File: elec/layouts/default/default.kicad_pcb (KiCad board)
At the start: 2 copper layers, 46.5 x 25.5 mm, 10 parts

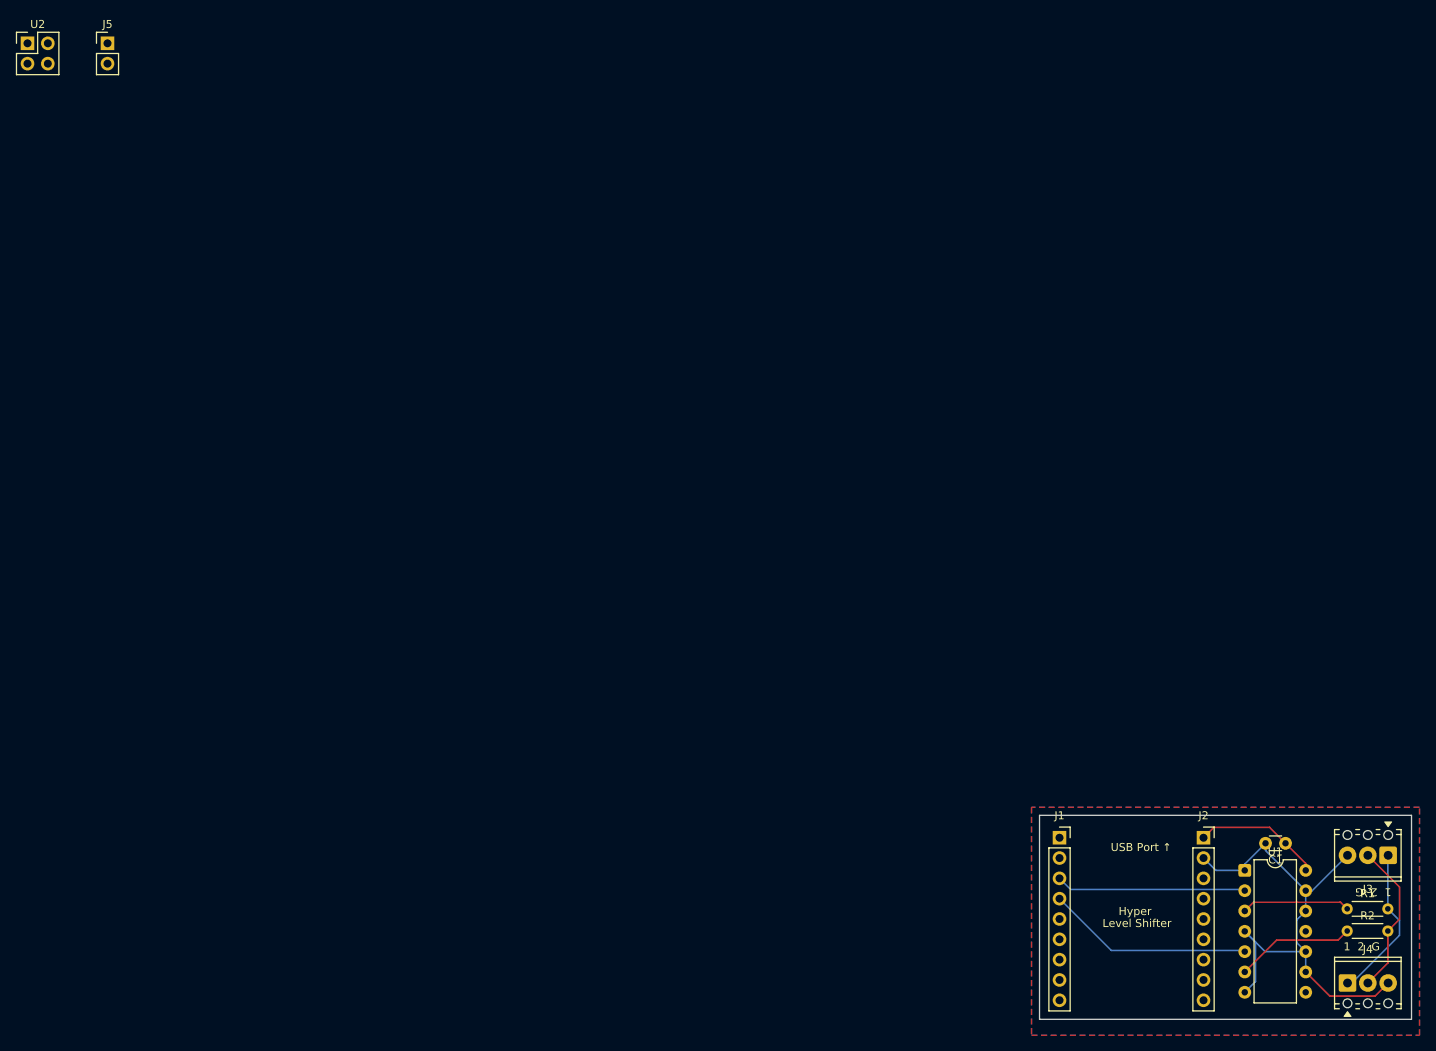
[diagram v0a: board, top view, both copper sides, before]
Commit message: PCB layout fixes, copper fill removal, and back silkscreen artwork
- Fix ESP32 header spacing: J1/J2 corrected to 15.5mm center-to-center
  (was 18mm, which matched castellated pads not through-hole pin rows)
- Shift J1/J2 right by 2.5mm to restore original gap to U1
- Remove GND copper fill (both layers) to fix WiFi antenna detuning
- Move J3/J4 screw terminals 1mm inward to clear silkscreen label overlap
- Update CLAUDE.md with corrected header spacing notes
- Add HyperHDR logo SVG (potrace-traced, evenodd fill) for B.SilkS import
- Back silkscreen text: "Hyper / ESP32 S3 / Level Shifter" between headers

Co-Authored-By: Claude Sonnet 4.6 <noreply@anthropic.com>
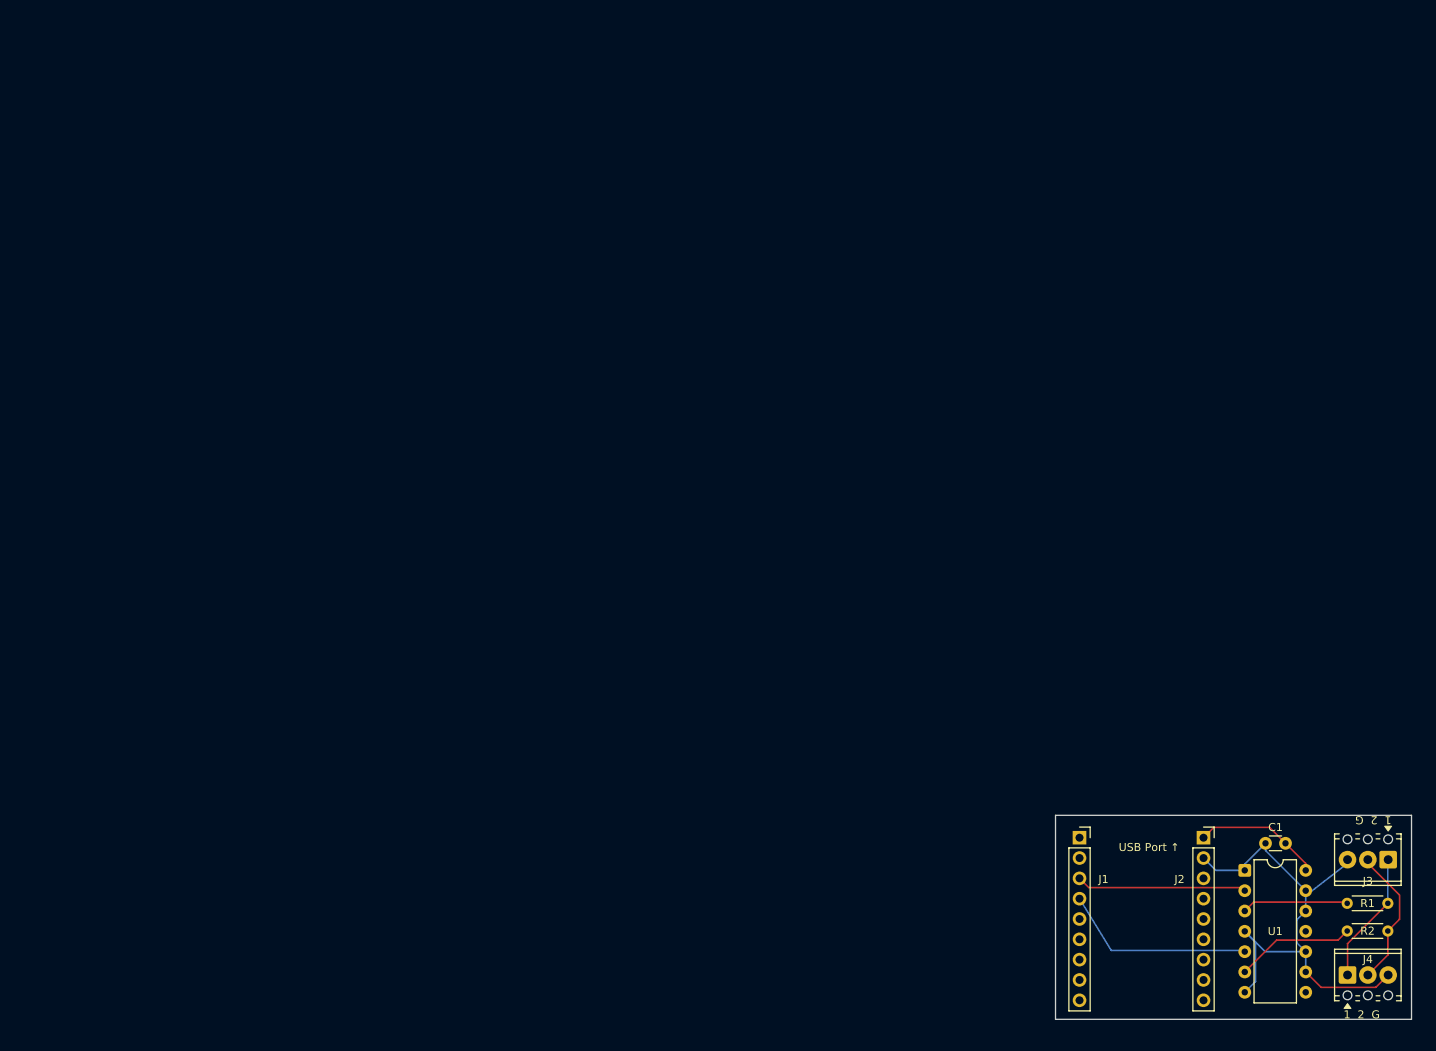
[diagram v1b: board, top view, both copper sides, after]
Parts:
- removed J5: , PowerConnector_1x2:PinHeader_1x02_P2.54mm_Vertical
- removed U2: , BuckModule_5V:PinHeader_2x02_P2.54mm_Vertical
- moved J1 2.50 mm to (131.5, 99.3)
- moved J4 1.00 mm to (165.0, 116.5)
- moved R1 0.69 mm to (165.0, 107.5)
- moved J3 0.54 mm to (170.1, 102.0)
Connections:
- C1 pad 1: 1 -> vcc_5v
- C1 pad 2: 2 -> 3
- J1 pad 3: 2-1 -> 2
- J2 pad 1: 1 -> vcc_5v
- J2 pad 2: 2 -> 3
- J3 pad 1: 1 -> 1-2
- J3 pad 2: 2-2 -> 2-1
- J3 pad 3: 2 -> 3
- J4 pad 1: 1 -> 1-2
- J4 pad 2: 2-3 -> 2-1
- J4 pad 3: 2 -> 3
- R1 pad 1: 1-1 -> 1
- R1 pad 2: 2-2 -> 1-2
- R2 pad 1: 1-2 -> 1-1
- R2 pad 2: 2-3 -> 2-1
- U1 pad 1: 2 -> 3
- U1 pad 10: 2 -> 3
- U1 pad 12: 2 -> 3
- U1 pad 13: 2 -> 3
- U1 pad 14: 1 -> vcc_5v
- U1 pad 2: 2-1 -> 2
- U1 pad 3: 1-1 -> 1
- U1 pad 4: 2 -> 3
- U1 pad 6: 1-2 -> 1-1
- U1 pad 7: 2 -> 3
- U1 pad 9: 2 -> 3
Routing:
- net 4: track 66.0 -> 0.00 mm
- net 3: track 0.00 -> 64.9 mm
- net 2: track 0.00 -> 21.5 mm
- net 23: track 19.6 -> 0.00 mm
- net 2-3: track 19.2 -> 0.00 mm
- net vcc_5v: track 0.00 -> 16.0 mm
- net 2-1: track 23.8 -> 17.2 mm
- net 1: track 16.0 -> 13.3 mm
- net 1-2: track 14.9 -> 16.6 mm
- net 5: track 25.9 -> 24.3 mm
- net 1-1: track 13.6 -> 14.9 mm
- removed copper zone on B.Cu, net 3
- removed copper zone on F.Cu, net 3
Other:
- board size 46.5 x 25.5 mm -> 44.5 x 25.5 mm
- board text added: "ESP32 S3"
